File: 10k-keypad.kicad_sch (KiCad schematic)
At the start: 41 parts, among them J1 AVR-ISP-6, K1 SW_Push, K10 SW_Push, K2 SW_Push, K3 SW_Push, K4 SW_Push, K5 SW_Push, K6 SW_Push, K7 SW_Push, K8 SW_Push, K9 SW_Push, SW1 SW_Push, U1 ATmega16U2-A, Y1 Crystal_GND24_Small

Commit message: finish schematic
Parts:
- added FB1: FerriteBead_Small, symbol Device:FerriteBead_Small
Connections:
- net GND: now also FB1.2
- new net Earth: FB1.1
- no-connect marks 2 -> 12
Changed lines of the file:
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@@
   (junction (at 254 135.89) (diameter 0) (color 0 0 0 0)
   )
+  (junction (at 69.85 175.26) (diameter 0) (color 0 0 0 0)
+  )
   (junction (at 179.07 130.81) (diameter 0) (color 0 0 0 0)
   )
@@
   (junction (at 63.5 43.18) (diameter 0) (color 0 0 0 0)
   )
+  (junction (at 54.61 149.86) (diameter 0) (color 0 0 0 0)
+  )
   (junction (at 262.89 135.89) (diameter 0) (color 0 0 0 0)
   )
@@
   (junction (at 80.01 157.48) (diameter 0) (color 0 0 0 0)
   )
+  (junction (at 72.39 149.86) (diameter 0) (color 0 0 0 0)
+  )
   (junction (at 254 140.97) (diameter 0) (color 0 0 0 0)
   )
@@
   (junction (at 43.18 38.1) (diameter 0) (color 0 0 0 0)
   )
+  (junction (at 76.2 181.61) (diameter 0) (color 0 0 0 0)
+  )
   (junction (at 104.14 38.1) (diameter 0) (color 0 0 0 0)
   )
@@
   (junction (at 58.42 38.1) (diameter 0) (color 0 0 0 0)
   )
+  (junction (at 82.55 185.42) (diameter 0) (color 0 0 0 0)
+  )
   (junction (at 62.23 175.26) (diameter 0) (color 0 0 0 0)
   )
@@
   (junction (at 88.9 38.1) (diameter 0) (color 0 0 0 0)
   )
+  (no_connect (at 199.39 77.47))
+  (no_connect (at 199.39 118.11))
+  (no_connect (at 199.39 115.57))
+  (no_connect (at 199.39 67.31))
+  (no_connect (at 199.39 120.65))
   (no_connect (at 46.99 167.64))
   (no_connect (at 46.99 152.4))
+  (no_connect (at 199.39 80.01))
+  (no_connect (at 199.39 113.03))
+  (no_connect (at 199.39 82.55))
+  (no_connect (at 199.39 110.49))
+  (no_connect (at 199.39 85.09))
   (wire (pts (xy 179.07 59.69) (xy 181.61 59.69))
     (stroke (width 0) (type default))
@@
     (stroke (width 0) (type default))
   )
+  (wire (pts (xy 82.55 181.61) (xy 82.55 185.42))
+    (stroke (width 0) (type default))
+  )
   (wire (pts (xy 63.5 43.18) (xy 78.74 43.18))
     (stroke (width 0) (type default))
@@
     (stroke (width 0) (type default))
   )
+  (wire (pts (xy 54.61 142.24) (xy 54.61 149.86))
+    (stroke (width 0) (type default))
+  )
   (wire (pts (xy 49.53 175.26) (xy 49.53 177.8))
     (stroke (width 0) (type default))
@@
     (stroke (width 0) (type default))
   )
-  (wire (pts (xy 102.87 185.42) (xy 69.85 185.42))
+  (wire (pts (xy 102.87 185.42) (xy 82.55 185.42))
     (stroke (width 0) (type default))
   )
@@
     (stroke (width 0) (type default))
   )
+  (wire (pts (xy 72.39 149.86) (xy 73.66 149.86))
+    (stroke (width 0) (type default))
+  )
   (wire (pts (xy 147.32 82.55) (xy 151.13 82.55))
     (stroke (width 0) (type default))
@@
     (stroke (width 0) (type default))
   )
-  (wire (pts (xy 52.07 149.86) (xy 58.42 149.86))
+  (wire (pts (xy 52.07 149.86) (xy 54.61 149.86))
     (stroke (width 0) (type default))
   )
@@
     (stroke (width 0) (type default))
   )
+  (wire (pts (xy 54.61 149.86) (xy 58.42 149.86))
+    (stroke (width 0) (type default))
+  )
   (wire (pts (xy 271.78 48.26) (xy 271.78 46.99))
     (stroke (width 0) (type default))
@@
     (stroke (width 0) (type default))
   )
+  (wire (pts (xy 82.55 185.42) (xy 69.85 185.42))
+    (stroke (width 0) (type default))
+  )
   (wire (pts (xy 257.81 116.84) (xy 261.62 116.84))
     (stroke (width 0) (type default))
@@
     (stroke (width 0) (type default))
   )
+  (wire (pts (xy 76.2 181.61) (xy 77.47 181.61))
+    (stroke (width 0) (type default))
+  )
   (wire (pts (xy 78.74 43.18) (xy 93.98 43.18))
     (stroke (width 0) (type default))
@@
     (stroke (width 0) (type default))
   )
-  (wire (pts (xy 67.31 149.86) (xy 73.66 149.86))
+  (wire (pts (xy 67.31 149.86) (xy 72.39 149.86))
     (stroke (width 0) (type default))
   )
@@
     )
   )
+  (symbol (lib_id "power:PWR_FLAG") (at 69.85 175.26 0) (unit 1)
+    (in_bom yes) (on_board yes) (dnp no) (fields_autoplaced)
+    (property "Reference" "#FLG02" (at 69.85 173.355 0)
+      (effects (font (size 1.27 1.27)) hide)
+    )
+    (property "Value" "PWR_FLAG" (at 69.85 170.18 0)
+      (effects (font (size 1.27 1.27)))
+    )
+    (property "Footprint" "" (at 69.85 175.26 0)
+      (effects (font (size 1.27 1.27)) hide)
+    )
+    (property "Datasheet" "~" (at 69.85 175.26 0)
+      (effects (font (size 1.27 1.27)) hide)
+    )
+    (pin "1")
+    (instances
+      (project "10k-keypad"
+        (path "/791ade27-e470-4262-a05c-a9d9b876a4df"
+          (reference "#FLG02") (unit 1)
+        )
+      )
+    )
+  )
   (symbol (lib_id "Device:D_Small") (at 63.5 40.64 90) (unit 1)
     (in_bom yes) (on_board yes) (dnp no)
@@
     )
   )
+  (symbol (lib_id "power:PWR_FLAG") (at 76.2 181.61 0) (unit 1)
+    (in_bom yes) (on_board yes) (dnp no) (fields_autoplaced)
+    (property "Reference" "#FLG04" (at 76.2 179.705 0)
+      (effects (font (size 1.27 1.27)) hide)
+    )
+    (property "Value" "PWR_FLAG" (at 76.2 176.53 0)
+      (effects (font (size 1.27 1.27)))
+    )
+    (property "Footprint" "" (at 76.2 181.61 0)
+      (effects (font (size 1.27 1.27)) hide)
+    )
+    (property "Datasheet" "~" (at 76.2 181.61 0)
+      (effects (font (size 1.27 1.27)) hide)
+    )
+    (pin "1")
+    (instances
+      (project "10k-keypad"
+        (path "/791ade27-e470-4262-a05c-a9d9b876a4df"
+          (reference "#FLG04") (unit 1)
+        )
+      )
+    )
+  )
   (symbol (lib_id "power:+5V") (at 73.66 149.86 0) (unit 1)
     (in_bom yes) (on_board yes) (dnp no) (fields_autoplaced)
@@
         (path "/791ade27-e470-4262-a05c-a9d9b876a4df"
           (reference "#PWR011") (unit 1)
+        )
+      )
+    )
+  )
+  (symbol (lib_id "Device:FerriteBead_Small") (at 80.01 181.61 90) (unit 1)
+    (in_bom yes) (on_board yes) (dnp no)
+    (property "Reference" "FB1" (at 80.01 177.8 90)
+      (effects (font (size 1.27 1.27)))
+    )
+    (property "Value" "FerriteBead_Small" (at 79.9719 177.8 90)
+      (effects (font (size 1.27 1.27)) hide)
+    )
+    (property "Footprint" "" (at 80.01 183.388 90)
+      (effects (font (size 1.27 1.27)) hide)
+    )
+    (property "Datasheet" "~" (at 80.01 181.61 0)
+      (effects (font (size 1.27 1.27)) hide)
+    )
+    (pin "1")
+    (pin "2")
+    (instances
+      (project "10k-keypad"
+        (path "/791ade27-e470-4262-a05c-a9d9b876a4df"
+          (reference "FB1") (unit 1)
         )
       )
@@
         (path "/791ade27-e470-4262-a05c-a9d9b876a4df"
           (reference "#PWR09") (unit 1)
+        )
+      )
+    )
+  )
+  (symbol (lib_id "power:PWR_FLAG") (at 72.39 149.86 180) (unit 1)
+    (in_bom yes) (on_board yes) (dnp no) (fields_autoplaced)
+    (property "Reference" "#FLG03" (at 72.39 151.765 0)
+      (effects (font (size 1.27 1.27)) hide)
+    )
+    (property "Value" "PWR_FLAG" (at 72.39 154.94 0)
+      (effects (font (size 1.27 1.27)))
+    )
+    (property "Footprint" "" (at 72.39 149.86 0)
+      (effects (font (size 1.27 1.27)) hide)
+    )
+    (property "Datasheet" "~" (at 72.39 149.86 0)
+      (effects (font (size 1.27 1.27)) hide)
+    )
+    (pin "1")
+    (instances
+      (project "10k-keypad"
+        (path "/791ade27-e470-4262-a05c-a9d9b876a4df"
+          (reference "#FLG03") (unit 1)
         )
       )
@@
         )
       )
+    )
+  )
+  (symbol (lib_id "power:Earth") (at 76.2 181.61 0) (unit 1)
+    (in_bom yes) (on_board yes) (dnp no) (fields_autoplaced)
+    (property "Reference" "#PWR016" (at 76.2 187.96 0)
+      (effects (font (size 1.27 1.27)) hide)
+    )
+    (property "Value" "Earth" (at 76.2 185.42 0)
+      (effects (font (size 1.27 1.27)) hide)
+    )
+    (property "Footprint" "" (at 76.2 181.61 0)
+      (effects (font (size 1.27 1.27)) hide)
+    )
+    (property "Datasheet" "~" (at 76.2 181.61 0)
+      (effects (font (size 1.27 1.27)) hide)
+    )
+    (pin "1")
+    (instances
+      (project "10k-keypad"
+        (path "/791ade27-e470-4262-a05c-a9d9b876a4df"
+          (reference "#PWR016") (unit 1)
+        )
+      )
+    )
+  )
+  (symbol (lib_id "power:PWR_FLAG") (at 54.61 142.24 0) (unit 1)
+    (in_bom yes) (on_board yes) (dnp no) (fields_autoplaced)
+    (property "Reference" "#FLG01" (at 54.61 140.335 0)
+      (effects (font (size 1.27 1.27)) hide)
+    )
+    (property "Value" "PWR_FLAG" (at 54.61 137.16 0)
+      (effects (font (size 1.27 1.27)))
+    )
+    (property "Footprint" "" (at 54.61 142.24 0)
+      (effects (font (size 1.27 1.27)) hide)
+    )
+    (property "Datasheet" "~" (at 54.61 142.24 0)
+      (effects (font (size 1.27 1.27)) hide)
+    )
+    (pin "1")
+    (instances
+      (project "10k-keypad"
+        (path "/791ade27-e470-4262-a05c-a9d9b876a4df"
+          (reference "#FLG01") (unit 1)
+        )
+      )

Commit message: footprints
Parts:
- C1, C2, C3, C4, C5, C6, C7, C8: footprint (none) -> Capacitor_SMD:C_0805_2012Metric_Pad1.18x1.45mm_HandSolder
- D10, D11, D2, D3, D4, D5, D6, D7, D8, D9: footprint (none) -> Diode_SMD:D_SOD-123
- F1: footprint (none) -> Fuse:Fuse_1206_3216Metric_Pad1.42x1.75mm_HandSolder
- FB1: footprint (none) -> Inductor_SMD:L_0805_2012Metric_Pad1.15x1.40mm_HandSolder
- J1: footprint (none) -> random-keyboard-parts:Reset_Pretty-Mask
- K1, K10, K2, K3, K4, K5, K6, K7, K8, K9: footprint (none) -> marbastlib-mx:SW_MX_HS_CPG151101S11_1u
- R1, R2, R3, R4, R5, R6: footprint (none) -> Resistor_SMD:R_0805_2012Metric_Pad1.20x1.40mm_HandSolder
- SW1: footprint (none) -> Button_Switch_SMD:SW_SPST_SKQG_WithStem
- USB1: footprint (none) -> Type-C:HRO-TYPE-C-31-M-12-HandSoldering
- Y1: footprint (none) -> Crystal:Crystal_SMD_3225-4Pin_3.2x2.5mm_HandSoldering

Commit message: crystal clock
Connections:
- net COL5: now also U1.8 (PD2); no longer U1.5 (PC2)
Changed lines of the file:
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@@
   (no_connect (at 199.39 113.03))
   (no_connect (at 199.39 82.55))
-  (no_connect (at 199.39 110.49))
   (no_connect (at 199.39 85.09))
+  (no_connect (at 199.39 90.17))
   (wire (pts (xy 179.07 59.69) (xy 181.61 59.69))
     (stroke (width 0) (type default))
@@
     )
   )
-  (global_label "COL5" (shape input) (at 199.39 90.17 0) (fields_autoplaced)
-    (effects (font (size 1.27 1.27)) (justify left))
-    (property "Intersheetrefs" "${INTERSHEET_REFS}" (at 207.2133 90.17 0)
-      (effects (font (size 1.27 1.27)) (justify left) hide)
-    )
+  (global_label "COL5" (shape input) (at 199.39 110.49 0) (fields_autoplaced)
+    (effects (font (size 1.27 1.27)) (justify left))
+    (property "Intersheetrefs" "${INTERSHEET_REFS}" (at 207.2133 110.49 0)
+      (effects (font (size 1.27 1.27)) (justify left) hide)
+    )

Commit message: finish routing
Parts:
- removed C5, C6, C7: 0.1u, Capacitor_SMD:C_0805_2012Metric_Pad1.18x1.45mm_HandSolder, symbol Device:C_Small
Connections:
- net COL1: now also U1.23 (PC6); no longer U1.26 (PC4)
- net COL2: now also U1.22 (PC7); no longer U1.25 (PC5)
- net COL3: now also U1.21 (PB7); no longer U1.23 (PC6)
- net COL4: now also U1.20 (PB6); no longer U1.22 (PC7)
- net Earth: now also USB1.13 (SHIELD)
- net GND: no longer USB1.13 (SHIELD)
- net ROW1: now also U1.9 (PD3); no longer U1.7 (PD1)
- net ROW2: now also U1.10 (PD4); no longer U1.6 (PD0)
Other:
- moved on the sheet: C4, C8

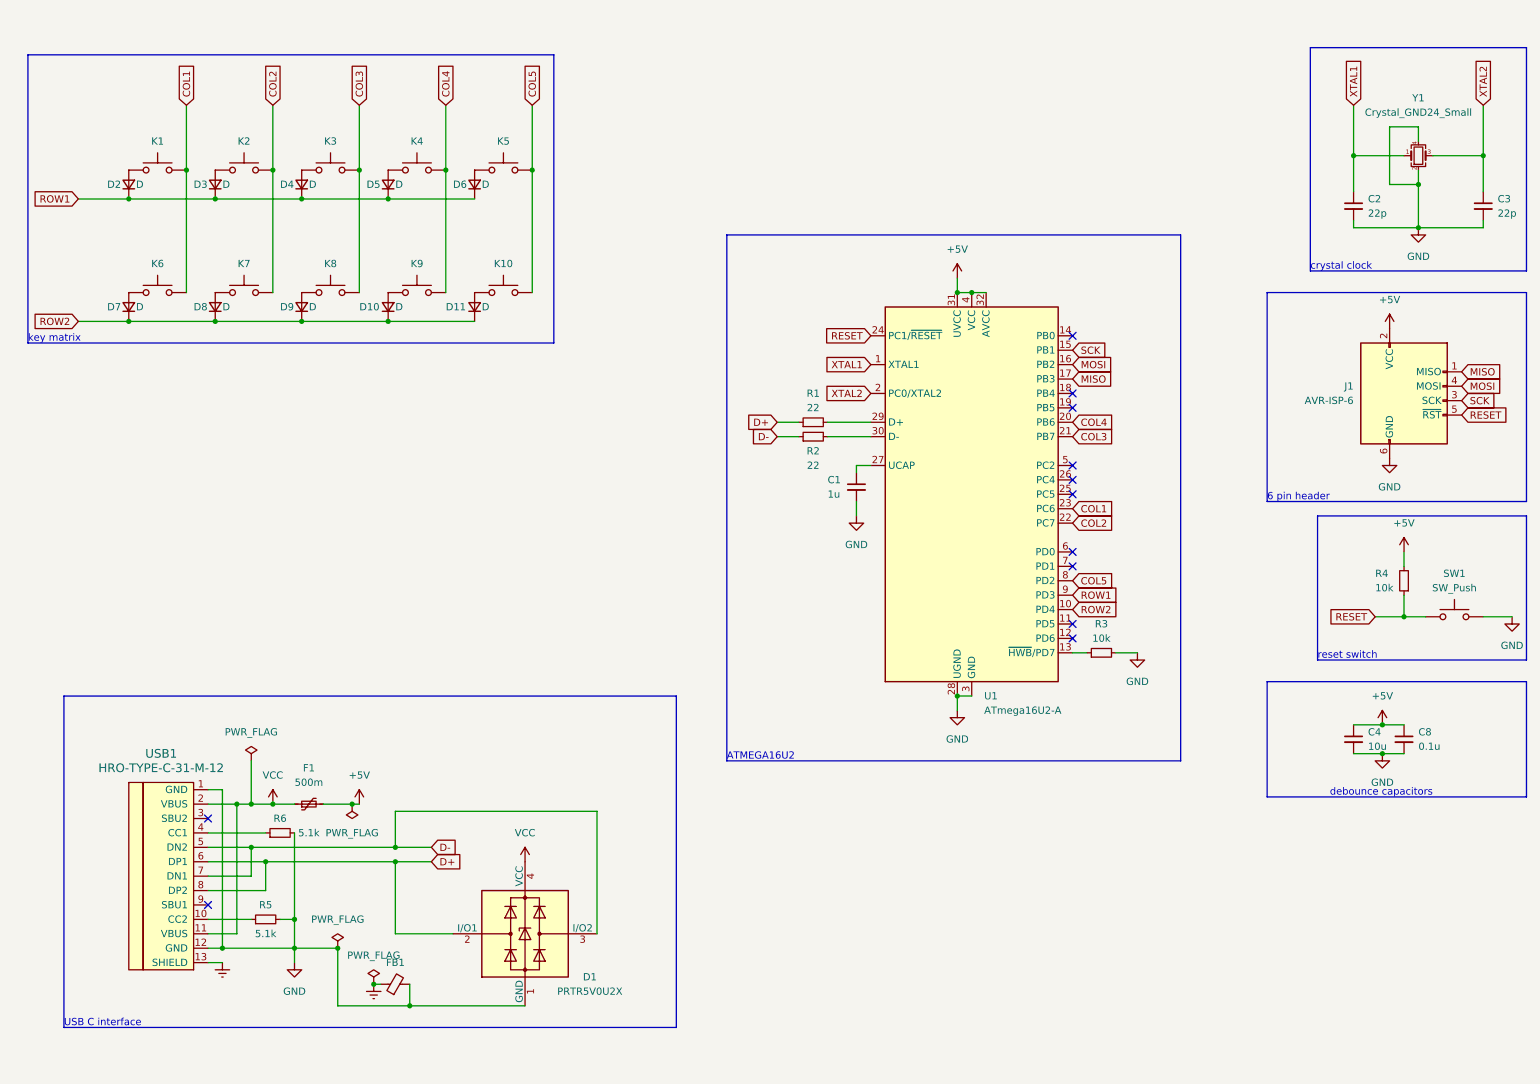
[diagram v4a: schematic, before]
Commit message: add hall sensors to schematic
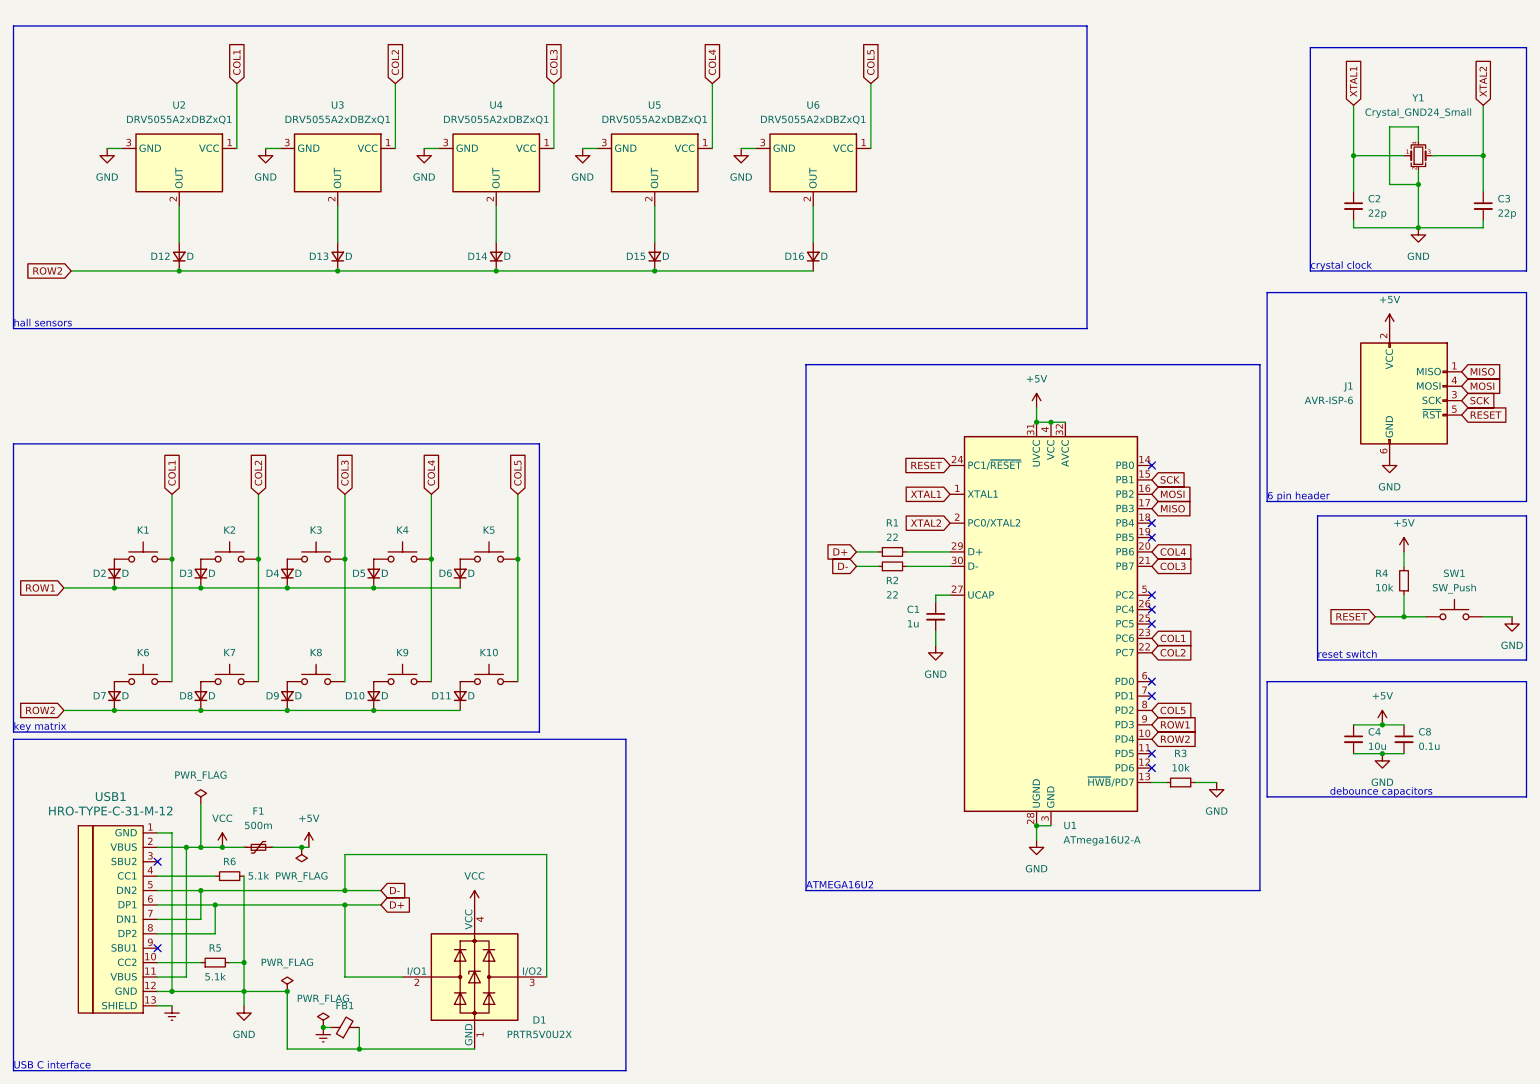
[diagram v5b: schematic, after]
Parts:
- added D12, D13, D14, D15, D16: D, Diode_SMD:D_SOD-123, symbol Device:D_Small
- added U2, U3, U4, U5, U6: DRV5055A2xDBZxQ1, Package_TO_SOT_SMD:SOT-23, symbol Sensor_Magnetic:DRV5055A2xDBZxQ1
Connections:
- net COL1: now also U2.1 (VCC)
- net COL2: now also U3.1 (VCC)
- net COL3: now also U4.1 (VCC)
- net COL4: now also U5.1 (VCC)
- net COL5: now also U6.1 (VCC)
- net GND: now also U2.3 (GND), U3.3 (GND), U4.3 (GND), U5.3 (GND), U6.3 (GND)
- net ROW2: now also D12.1 (K), D13.1 (K), D14.1 (K), D15.1 (K), D16.1 (K)
- new net: D14.2 (A), U4.2 (OUT)
- new net: D13.2 (A), U3.2 (OUT)
- new net: D12.2 (A), U2.2 (OUT)
- new net: D16.2 (A), U6.2 (OUT)
- new net: D15.2 (A), U5.2 (OUT)
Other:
- note added: "hall sensors"
- moved on the sheet: C1, D1, D10, D11, D2, D3, D4, D5, D6, D7, D8, D9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

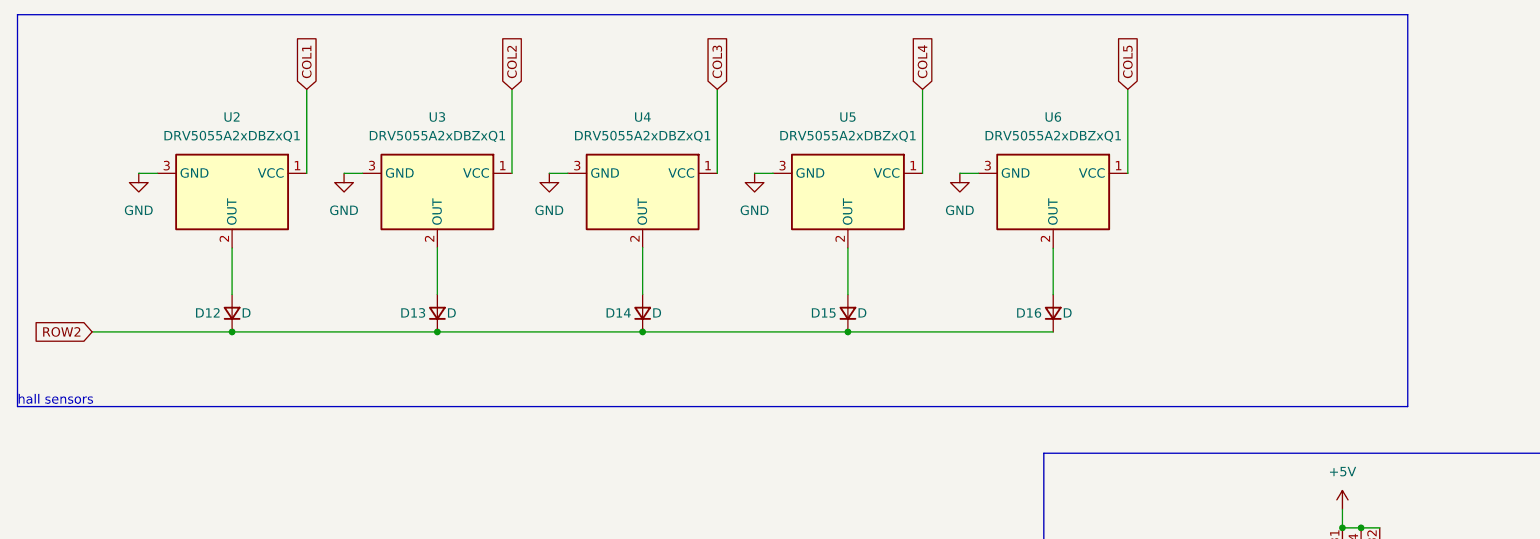
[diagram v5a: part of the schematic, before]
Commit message: complete hall sensor schematic
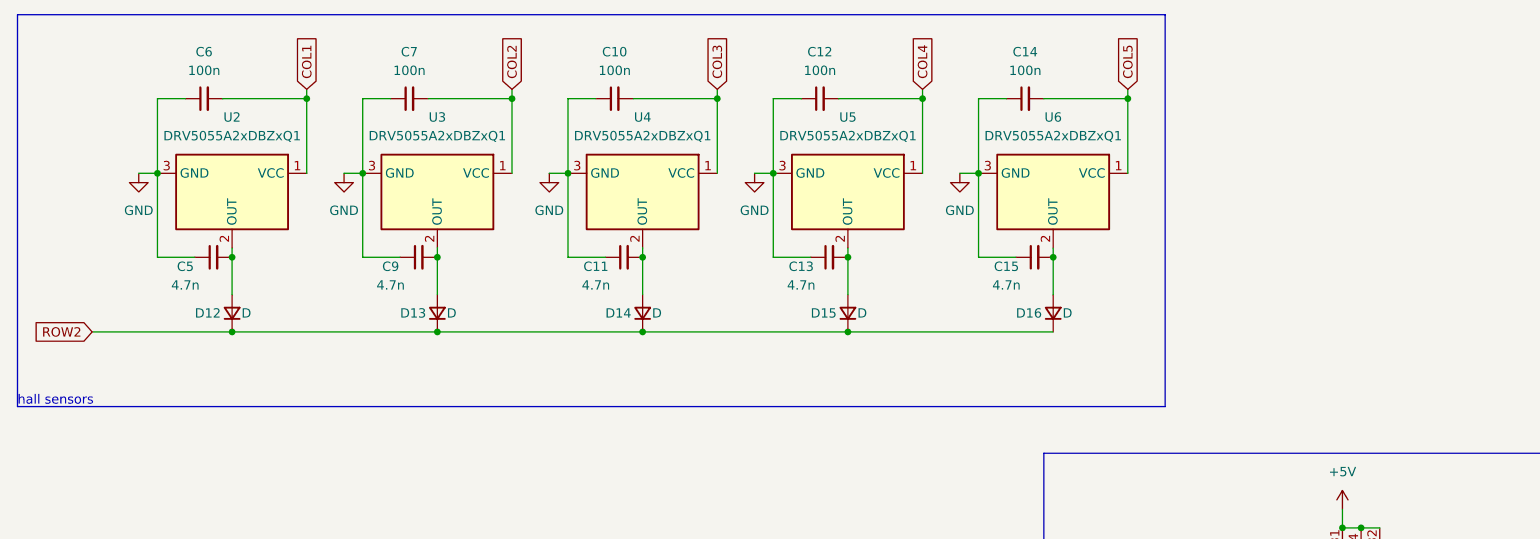
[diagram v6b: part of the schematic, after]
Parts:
- added C10, C12, C14, C6, C7: 100n, symbol Device:C_Small
- added C11, C13, C15, C5, C9: 4.7n, symbol Device:C_Small
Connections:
- net COL1: now also C6.2
- net COL2: now also C7.2
- net COL3: now also C10.2
- net COL4: now also C12.2
- net COL5: now also C14.2
- net GND: now also C10.1, C11.1, C12.1, C13.1, C14.1, C15.1, C5.1, C6.1, C7.1, C9.1
- net at D14.2 (A), U4.2 (OUT): now also C11.2
- net at D13.2 (A), U3.2 (OUT): now also C9.2
- net at D12.2 (A), U2.2 (OUT): now also C5.2
- net at D16.2 (A), U6.2 (OUT): now also C15.2
- net at D15.2 (A), U5.2 (OUT): now also C13.2
